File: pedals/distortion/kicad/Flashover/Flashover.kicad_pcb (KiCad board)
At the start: 4 copper layers, 87.6 x 84 mm, 95 parts, among them J1 Input, J2 Output, J3 9V DC, J4 SWD, J5 MIDI In, J6 MIDI Out, J7 To control board, K1 G6K-2F-Y 5VDC, K2 G6K-2F-Y 5VDC, Q1 MMBT3904, Q2 MMBT3904, SW5 Footswitch, U1 LM741, U11 H11L1, U2 TL072, U3 L7805, U4 RP2040, U5 W25Q16JVSS, U6 AP2112K-3.3, U7 MCP45HV51-104, U8 MCP45HV51-103, U9 MCP45HV51-103, Y1 12MHz

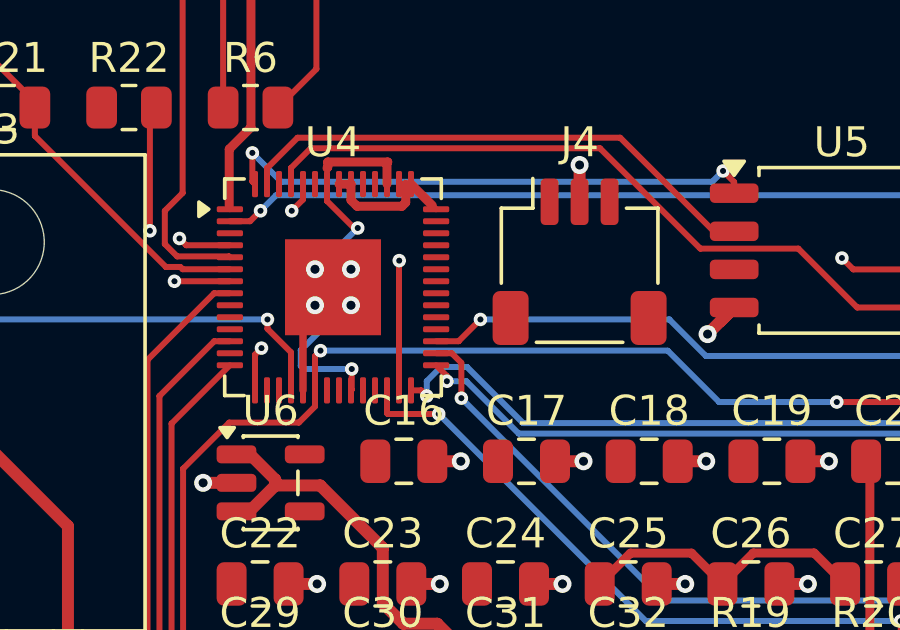
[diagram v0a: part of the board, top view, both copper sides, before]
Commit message: Hand-route SWDIO and SWCLK on the Flashover main board; note progress
Co-Authored-By: Claude Opus 5.5 <noreply@anthropic.com>
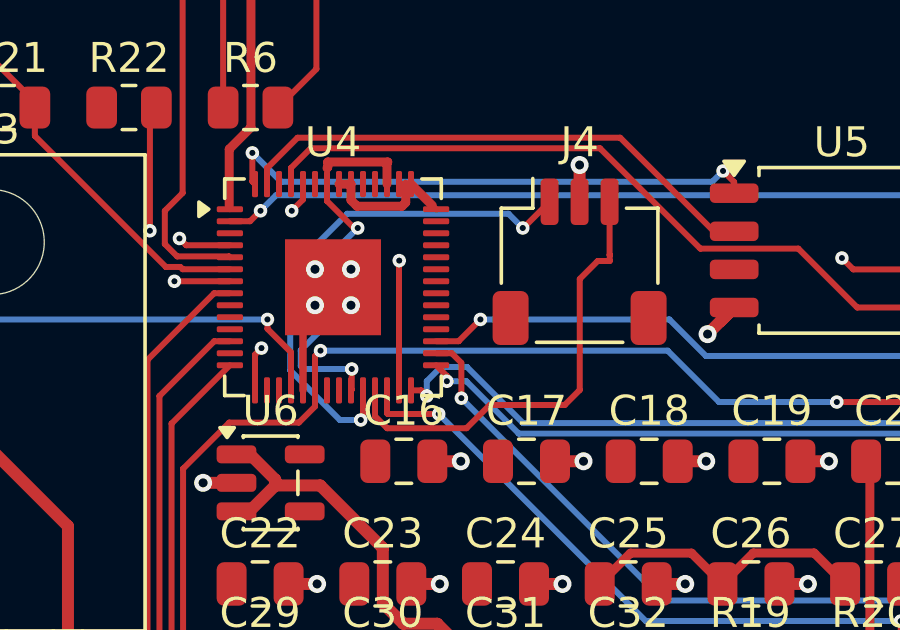
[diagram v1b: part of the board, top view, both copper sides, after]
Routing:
- net /Controller/SWCLK: track 0.00 -> 17.4 mm, vias 0 -> 2
- net /Controller/SWDIO: track 0.00 -> 15.3 mm
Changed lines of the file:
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@@
+	)
+	(segment
+		(start 141 113.7)
+		(end 141.02 113.7)
+		(width 0.2)
+		(layer "F.Cu")
+		(net "/Controller/SWCLK")
+	)
+	(segment
+		(start 135.675 119.1125)
+		(end 135.675 120.025)
+		(width 0.2)
+		(layer "F.Cu")
+		(net "/Controller/SWCLK")
+	)
+	(segment
+		(start 141.02 113.7)
+		(end 141.895 112.825)
+		(width 0.2)
+		(layer "F.Cu")
+		(net "/Controller/SWCLK")
+	)
+	(segment
+		(start 135.675 120.025)
+		(end 135.6 120.1)
+		(width 0.2)
+		(layer "F.Cu")
+		(net "/Controller/SWCLK")
+	)
+	(via
+		(at 141 113.7)
+		(size 0.45)
+		(drill 0.2)
+		(layers "F.Cu" "B.Cu")
+		(net "/Controller/SWCLK")
+	)
+	(via
+		(at 135.6 120.1)
+		(size 0.45)
+		(drill 0.2)
+		(layers "F.Cu" "B.Cu")
+		(net "/Controller/SWCLK")
+	)
+	(segment
+		(start 140.524998 113.224998)
+		(end 141 113.7)
+		(width 0.2)
+		(layer "B.Cu")
+		(net "/Controller/SWCLK")
+	)
+	(segment
+		(start 135.6 120.1)
+		(end 134.905025 120.1)
+		(width 0.2)
+		(layer "B.Cu")
+		(net "/Controller/SWCLK")
+	)
+	(segment
+		(start 133.25 118.444975)
+		(end 133.25 115.122182)
+		(width 0.2)
+		(layer "B.Cu")
+		(net "/Controller/SWCLK")
+	)
+	(segment
+		(start 133.25 115.122182)
+		(end 135.147184 113.224998)
+		(width 0.2)
+		(layer "B.Cu")
+		(net "/Controller/SWCLK")
+	)
+	(segment
+		(start 135.147184 113.224998)
+		(end 140.524998 113.224998)
+		(width 0.2)
+		(layer "B.Cu")
+		(net "/Controller/SWCLK")
+	)
+	(segment
+		(start 134.905025 120.1)
+		(end 133.25 118.444975)
+		(width 0.2)
+		(layer "B.Cu")
+		(net "/Controller/SWCLK")
+	)
+	(segment
+		(start 136.480025 120.375)
+		(end 139.125 120.375)
+		(width 0.2)
+		(layer "F.Cu")
+		(net "/Controller/SWDIO")
+	)
+	(segment
+		(start 143.9 114.6)
+		(end 143.895 114.595)
+		(width 0.2)
+		(layer "F.Cu")
+		(net "/Controller/SWDIO")
+	)
+	(segment
+		(start 143.895 114.595)
+		(end 143.895 112.825)
+		(width 0.2)
+		(layer "F.Cu")
+		(net "/Controller/SWDIO")
+	)
+	(segment
+		(start 142.9 115.4)
+		(end 143.5 114.8)
+		(width 0.2)
+		(layer "F.Cu")
+		(net "/Controller/SWDIO")
+	)
+	(segment
+		(start 139.9 119.6)
+		(end 142.4 119.6)
+		(width 0.2)
+		(layer "F.Cu")
+		(net "/Controller/SWDIO")
+	)
+	(segment
+		(start 136.075 119.1125)
+		(end 136.075 119.969975)
+		(width 0.2)
+		(layer "F.Cu")
+		(net "/Controller/SWDIO")
+	)
+	(segment
+		(start 142.4 119.6)
+		(end 142.9 119.1)
+		(width 0.2)
+		(layer "F.Cu")
+		(net "/Controller/SWDIO")
+	)
+	(segment
+		(start 143.9 114.8)
+		(end 143.9 114.6)
+		(width 0.2)
+		(layer "F.Cu")
+		(net "/Controller/SWDIO")
+	)
+	(segment
+		(start 139.125 120.375)
+		(end 139.9 119.6)
+		(width 0.2)
+		(layer "F.Cu")
+		(net "/Controller/SWDIO")
+	)
+	(segment
+		(start 136.075 119.969975)
+		(end 136.480025 120.375)
+		(width 0.2)
+		(layer "F.Cu")
+		(net "/Controller/SWDIO")
+	)
+	(segment
+		(start 143.5 114.8)
+		(end 143.9 114.8)
+		(width 0.2)
+		(layer "F.Cu")
+		(net "/Controller/SWDIO")
+	)
+	(segment
+		(start 142.9 119.1)
+		(end 142.9 115.4)
+		(width 0.2)
+		(layer "F.Cu")
+		(net "/Controller/SWDIO")
 	)
 	(segment

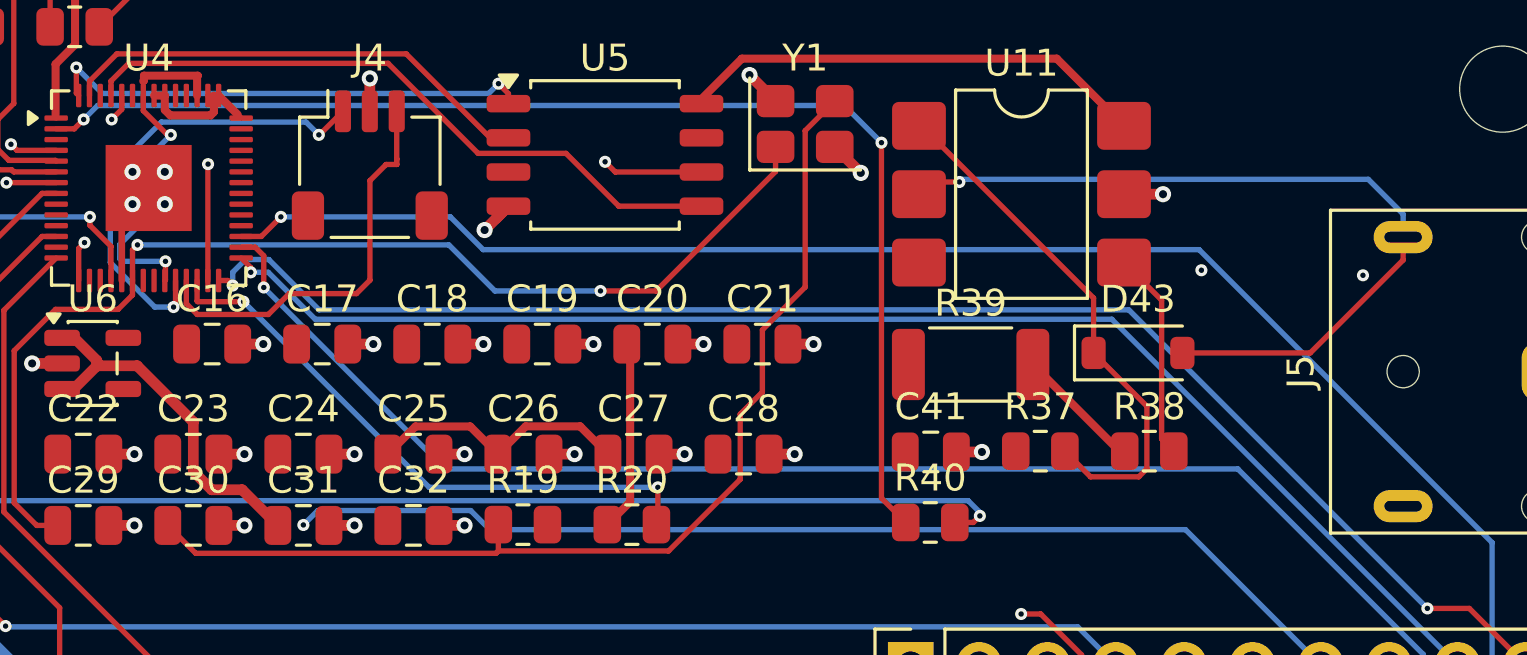
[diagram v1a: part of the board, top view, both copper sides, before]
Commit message: Hand-route MODE_BTN and the last +1V1 link; U4's bottom pins done
Co-Authored-By: Claude Opus 5.5 <noreply@anthropic.com>
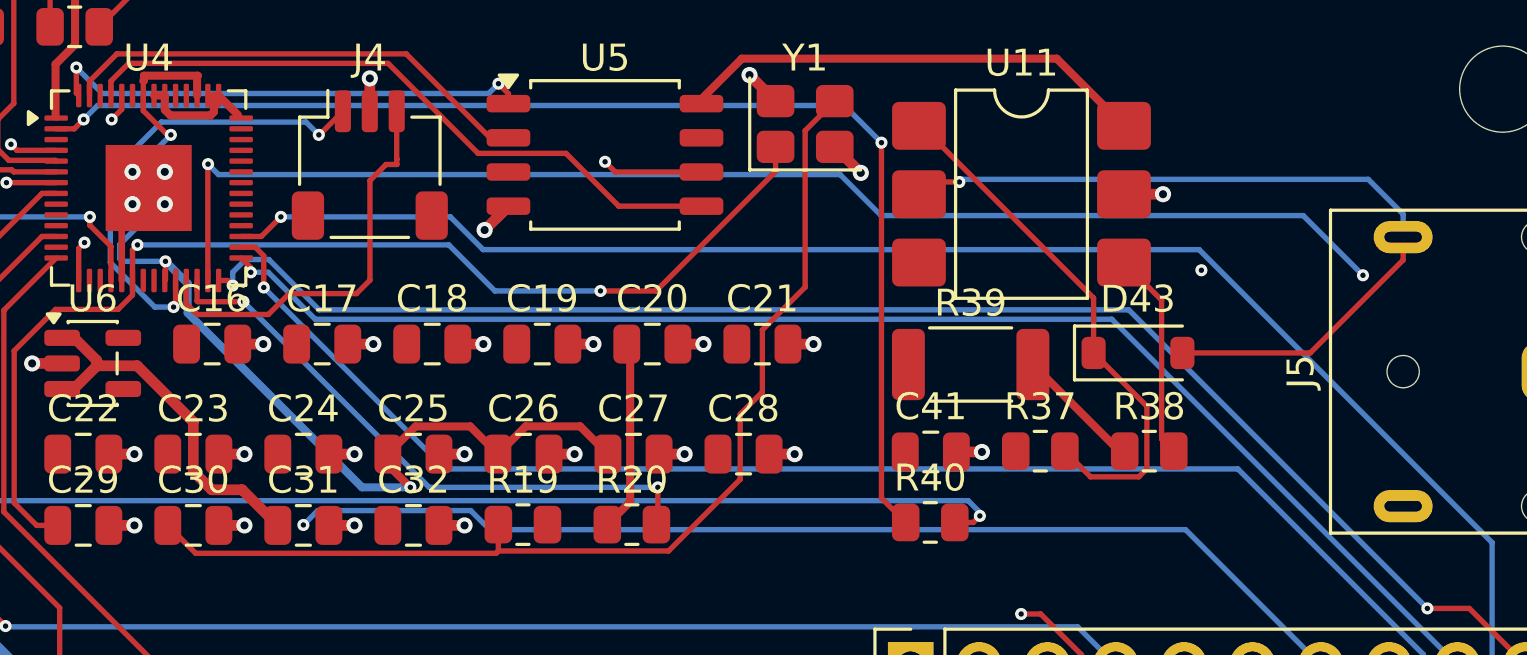
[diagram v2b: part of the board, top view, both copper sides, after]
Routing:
- net MODE_BTN: track 21.9 -> 66.5 mm
- net /Controller/+1V1: track 22.7 -> 37.5 mm, vias 2 -> 3
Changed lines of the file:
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@@
+	)
+	(segment
+		(start 143.565 125.965)
+		(end 144.4 126.8)
+		(width 0.3)
+		(layer "F.Cu")
+		(net "/Controller/+1V1")
+	)
+	(segment
+		(start 143.565 125.565)
+		(end 143.565 125.965)
+		(width 0.3)
+		(layer "F.Cu")
+		(net "/Controller/+1V1")
 	)
 	(segment
@@
 	)
 	(via
+		(at 144.4 126.8)
+		(size 0.45)
+		(drill 0.2)
+		(layers "F.Cu" "B.Cu")
+		(net "/Controller/+1V1")
+	)
+	(via
 		(at 135.5 113.699998)
 		(size 0.45)
@@
 	)
 	(segment
+		(start 142.607537 126.8)
+		(end 136.125 120.317463)
+		(width 0.3)
+		(layer "B.Cu")
+		(net "/Controller/+1V1")
+	)
+	(segment
 		(start 133.6 117.775448)
 		(end 133.6 118.3)
@@
 	)
 	(segment
+		(start 136.125 119.225)
+		(end 135.3 118.4)
+		(width 0.3)
+		(layer "B.Cu")
+		(net "/Controller/+1V1")
+	)
+	(segment
 		(start 133.7 118.4)
 		(end 135.3 118.4)
@@
 	)
 	(segment
+		(start 144.4 126.8)
+		(end 142.607537 126.8)
+		(width 0.3)
+		(layer "B.Cu")
+		(net "/Controller/+1V1")
+	)
+	(segment
+		(start 136.125 120.317463)
+		(end 136.125 119.225)
+		(width 0.3)
+		(layer "B.Cu")
+		(net "/Controller/+1V1")
+	)
+	(segment
 		(start 175.85 80.35)
 		(end 175.85 82.145)
@@
 		(net "MODE_BTN")
 	)
+	(segment
+		(start 136.8826 114.7872)
+		(end 137.271 115.1756)
+		(width 0.2)
+		(layer "B.Cu")
+		(net "MODE_BTN")
+	)
+	(segment
+		(start 160.3756 115.1756)
+		(end 161.9 116.7)
+		(width 0.2)
+		(layer "B.Cu")
+		(net "MODE_BTN")
+	)
+	(segment
+		(start 161.9 116.7)
+		(end 177.5879 116.7)
+		(width 0.2)
+		(layer "B.Cu")
+		(net "MODE_BTN")
+	)
+	(segment
+		(start 177.5879 116.7)
+		(end 179.807 118.9191)
+		(width 0.2)
+		(layer "B.Cu")
+		(net "MODE_BTN")
+	)
+	(segment
+		(start 137.271 115.1756)
+		(end 160.3756 115.1756)
+		(width 0.2)
+		(layer "B.Cu")
+		(net "MODE_BTN")
+	)

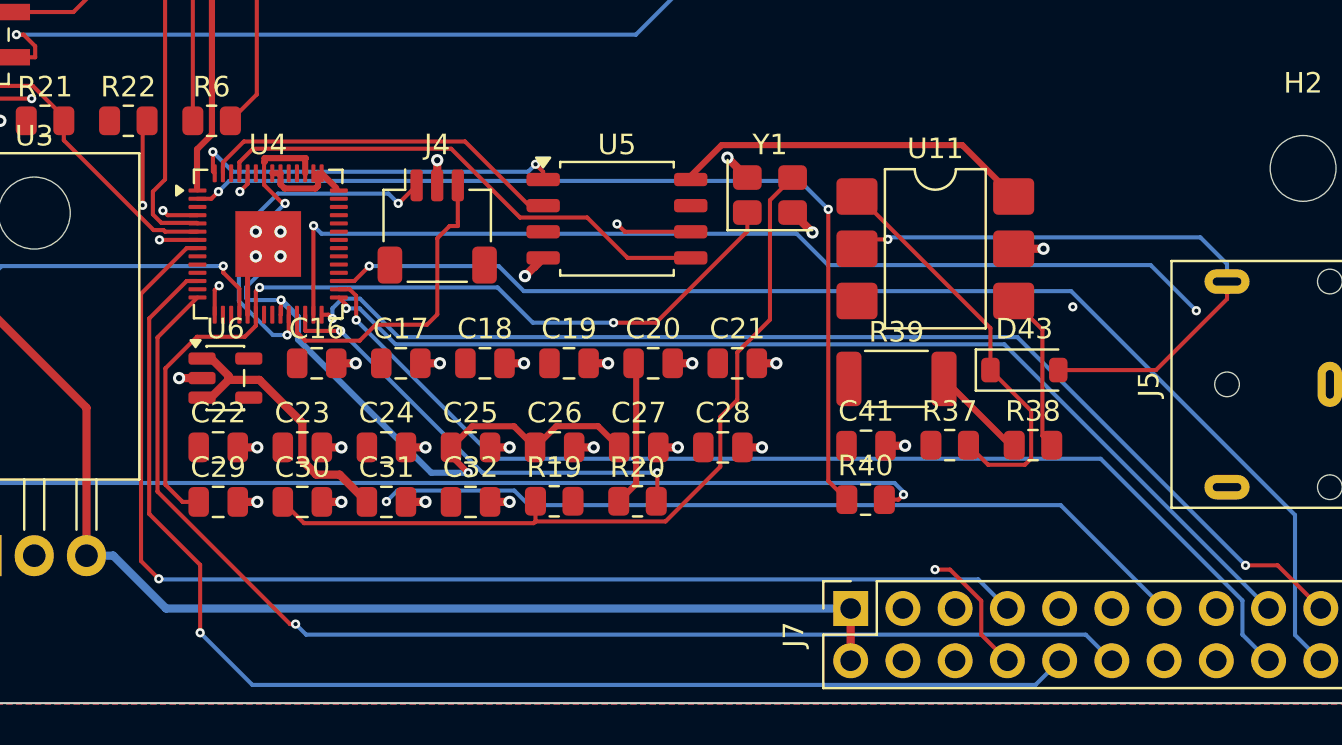
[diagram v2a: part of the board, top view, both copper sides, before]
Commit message: Move the Flashover crystal group next to U4 and the 3.3 V regulator to J7
Y1, R19, C29 and C30 now sit under U4's XIN/XOUT pins, cutting the crystal
tracks from about 25 mm to under 6 mm. U6 and its caps move to the free spot
beside J7, next to +5V and +3V3. The autorouter's tracks on the moved parts
were removed, and the crystal and LEVEL_B/LEVEL_SW lines rerouted.

Co-Authored-By: Claude Opus 5.5 <noreply@anthropic.com>
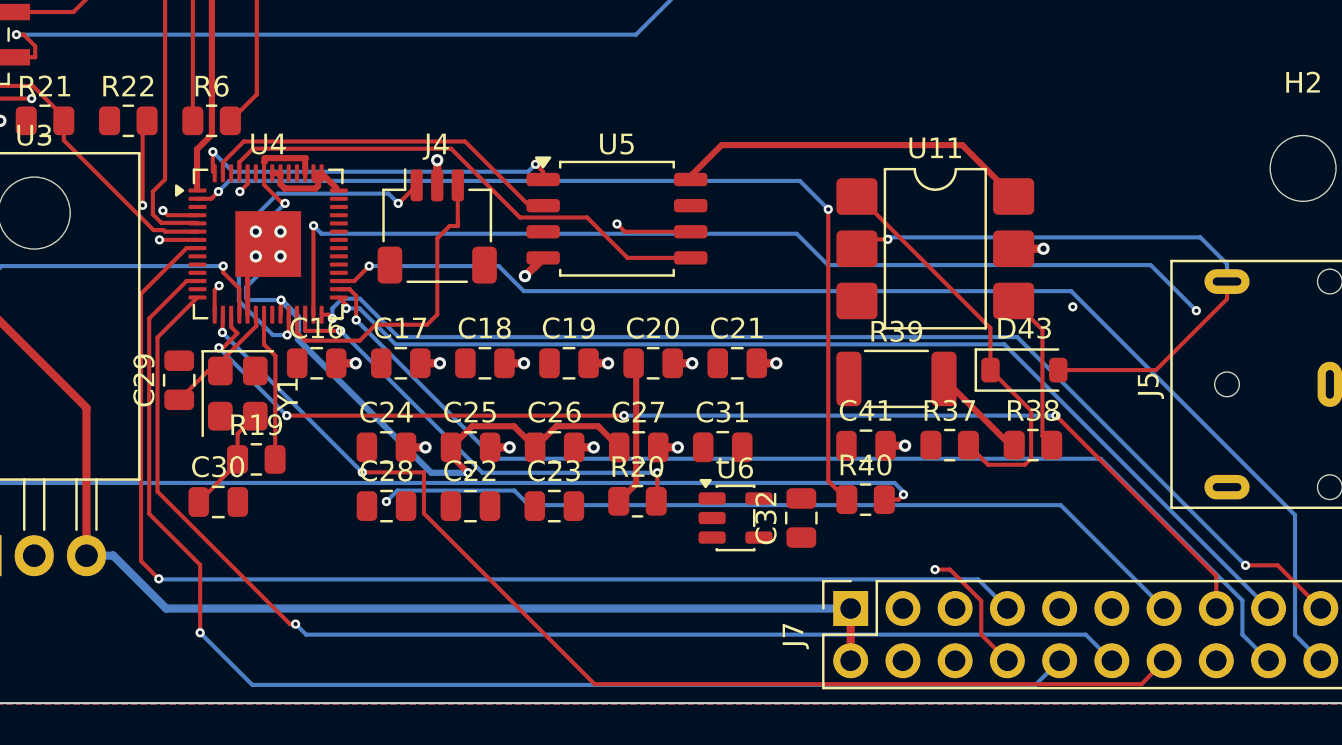
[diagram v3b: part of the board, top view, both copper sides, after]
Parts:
- moved Y1 27.6 mm to (133.2, 123.0), turned to -90 degrees
- moved U6 25.7 mm to (157.4, 129.0)
- moved C28 16.6 mm to (140.4, 128.4)
- moved C31 16.6 mm to (156.8, 125.6)
- moved C32 16.1 mm to (160.6, 129.0), turned to 90 degrees
- moved R19 14.6 mm to (134.1, 126.2)
- moved C22 12.6 mm to (144.5, 128.4)
- moved C23 12.6 mm to (148.6, 128.4)
- moved C29 6.21 mm to (130.3, 122.3), turned to 90 degrees
- moved C30 4.09 mm to (132.2, 128.2)
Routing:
- net LEVEL_SW: track 0.00 -> 56.9 mm, vias 0 -> 4
- net LEVEL_B: track 0.00 -> 55.4 mm, vias 0 -> 2
- net /Controller/XIN: track 42.0 -> 6.04 mm, vias 2 -> 0
- net Net-(C30-Pad1): track 39.3 -> 5.31 mm
- net +5V: track 184.6 -> 170.9 mm
- net GND: track 67.2 -> 56.7 mm, vias 60 -> 50
- net /Controller/XOUT: track 0.00 -> 7.27 mm

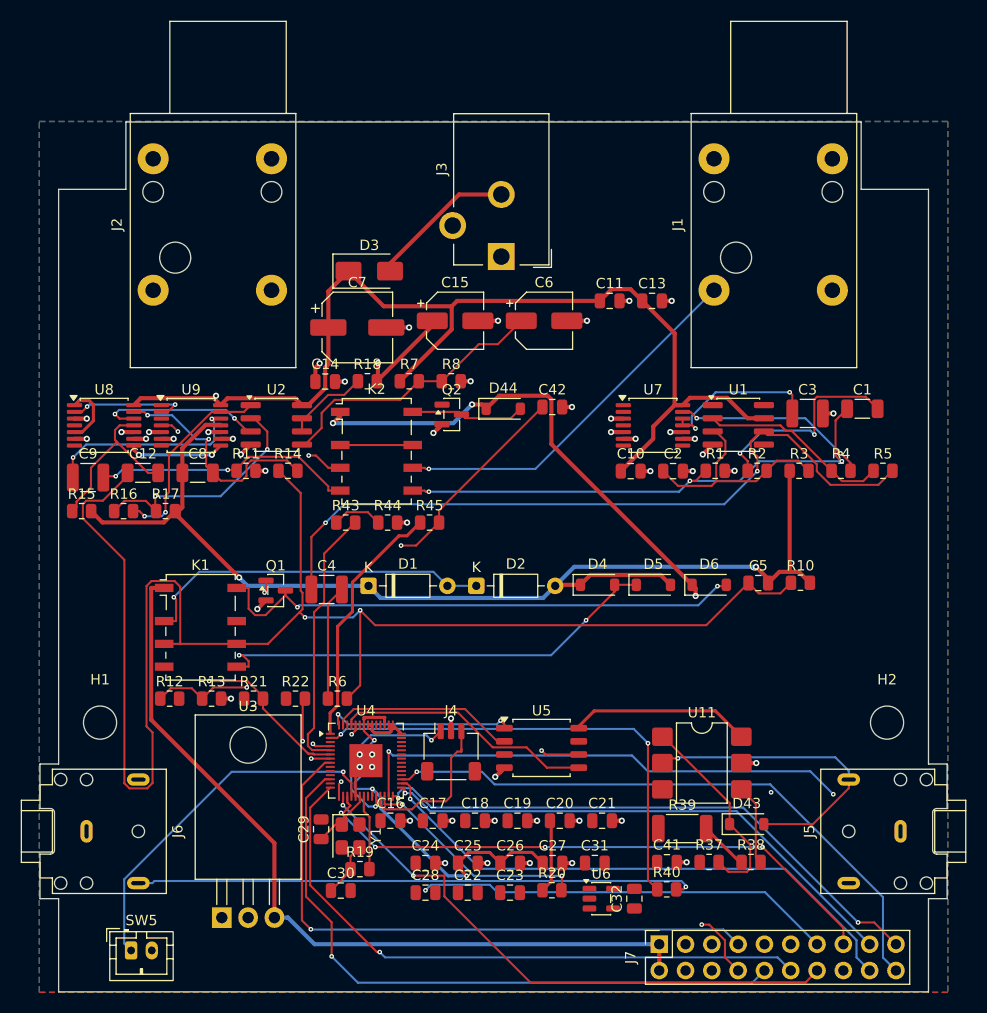
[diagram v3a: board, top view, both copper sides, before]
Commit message: Add the planned Flashover main board tracks (48 -> 9 open)
Each track was found by the two-layer search in scripts/build and checked with
DRC on a scratch copy before going in.

Co-Authored-By: Claude Opus 5.5 <noreply@anthropic.com>
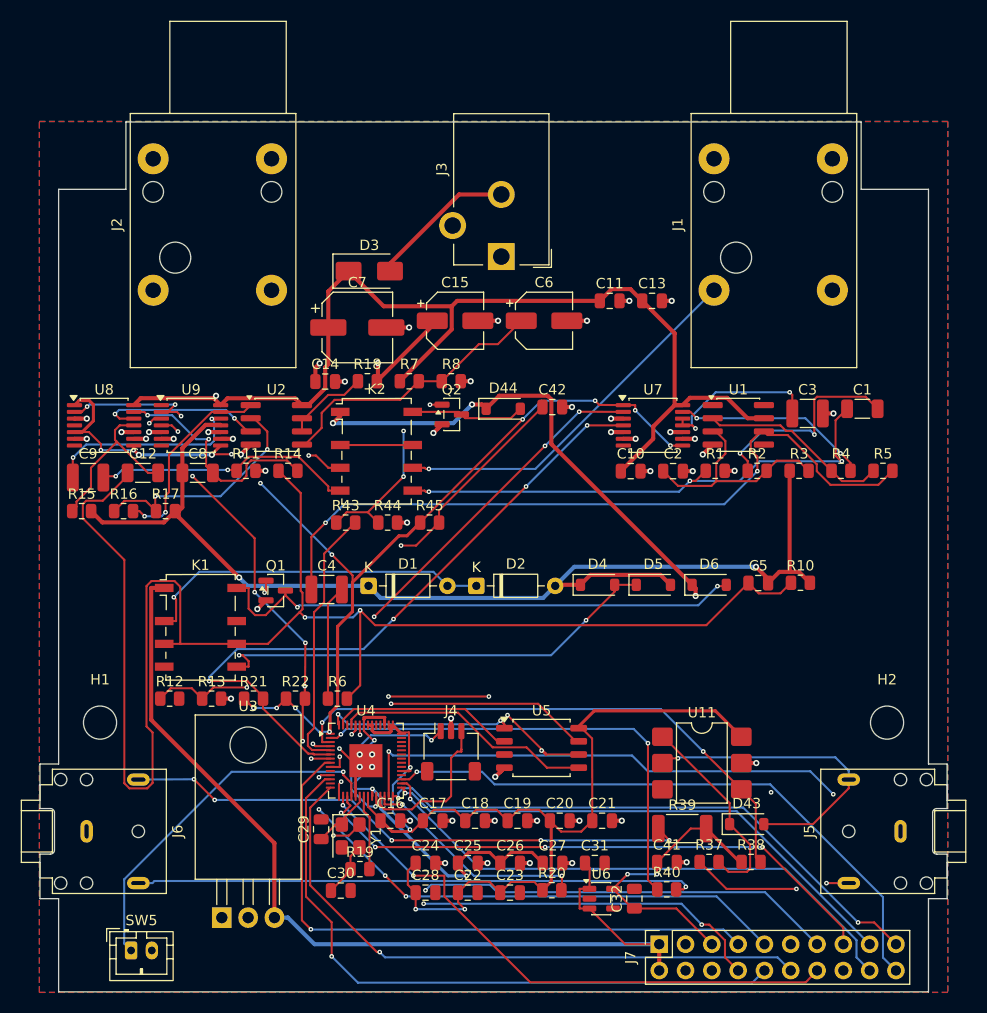
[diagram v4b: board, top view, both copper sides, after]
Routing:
- net +3V3: track 74.4 -> 251.1 mm, vias 2 -> 22
- net SCL: track 19.7 -> 98.1 mm, vias 4 -> 12
- net Net-(J6-PadR): track 0.00 -> 55.3 mm, vias 0 -> 5
- net GAIN_SW: track 0.00 -> 52.7 mm, vias 0 -> 4
- net SDA: track 42.5 -> 92.9 mm, vias 2 -> 5
- net GAIN_B: track 6.32 -> 53.8 mm, vias 1 -> 3
- net MIDI_RX: track 7.78 -> 54.7 mm, vias 0 -> 2
- net Net-(U4-QSPI_SD3): track 0.00 -> 24.8 mm, vias 0 -> 2
- net Net-(U4-QSPI_SCLK): track 4.79 -> 27.5 mm, vias 2 -> 5
- net GND: track 56.7 -> 73.8 mm, vias 50 -> 52
- net Net-(J5-PadR): track 0.00 -> 15.7 mm, vias 0 -> 2
- net +5V: track 170.9 -> 185.5 mm
- net Net-(Q2-B): track 4.88 -> 18.9 mm, vias 0 -> 3
